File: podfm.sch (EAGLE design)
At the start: 30 parts, among them IC1 ATMEGA168-AU, IC2 FT232RL, X1 MINI-USB-32005-301, X2 R141426

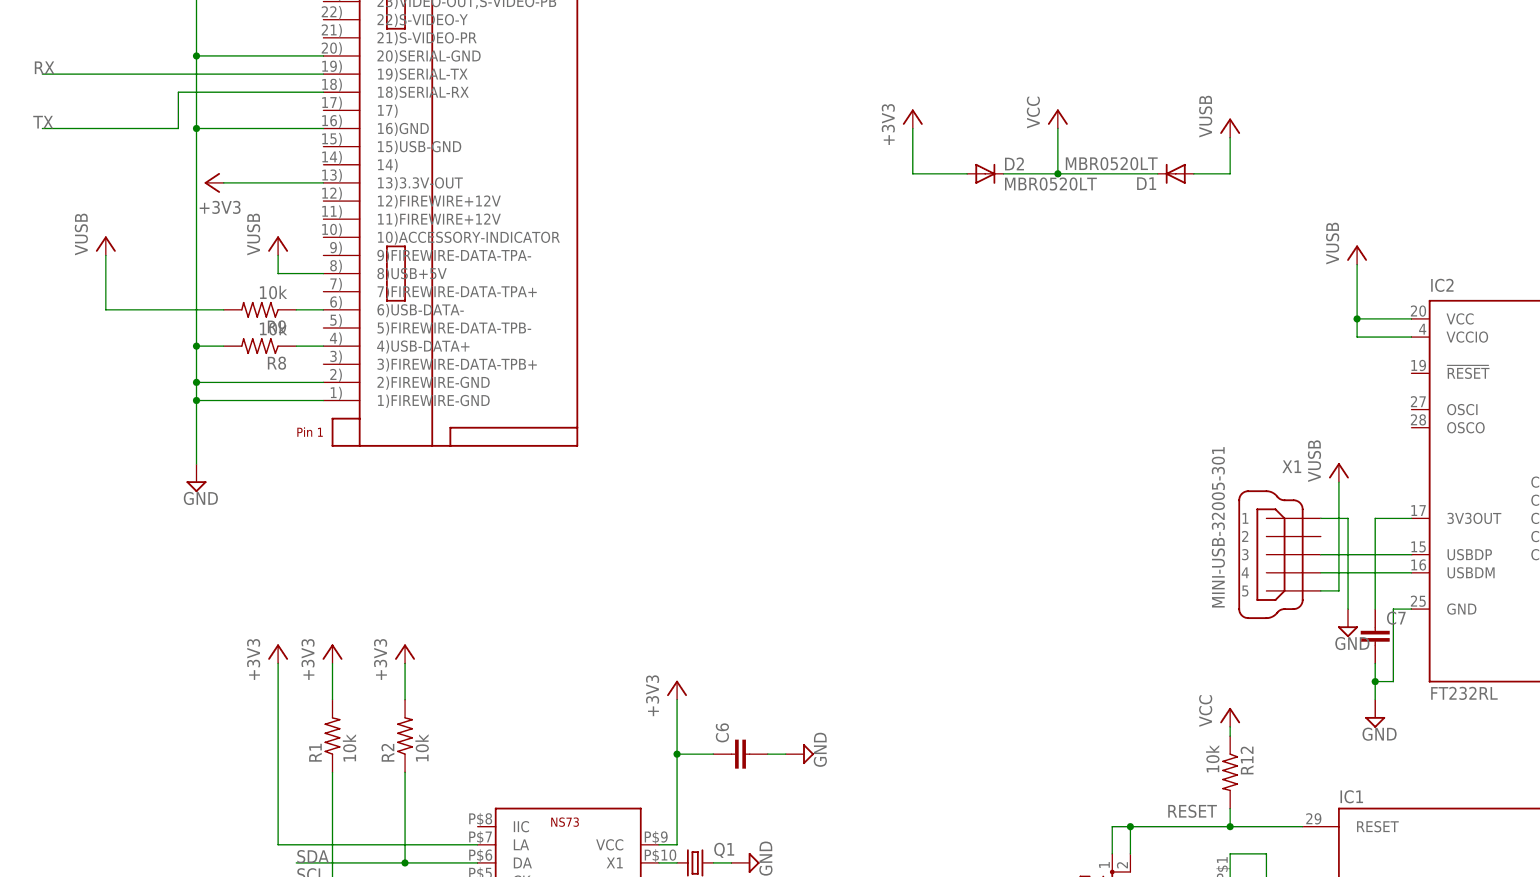
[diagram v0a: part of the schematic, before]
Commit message: 9/22/2013 fixed usb connection 1-VCC 2-data- 3-data+ 5-GND added resistor network for ipod iphone charging Signed-off-by: goose1987 <phamh1987@gmail.com>
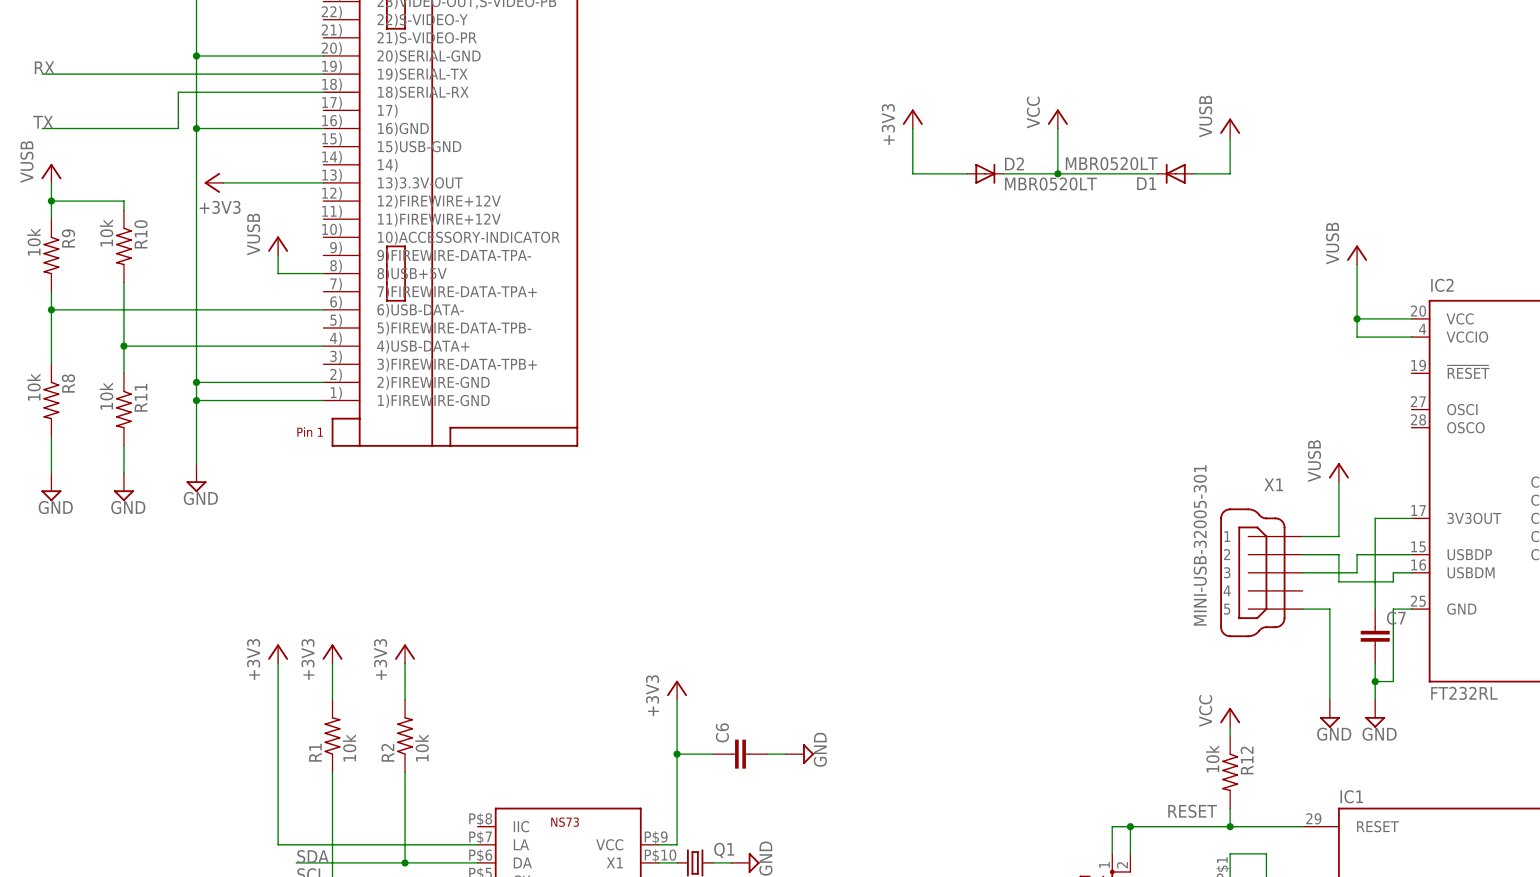
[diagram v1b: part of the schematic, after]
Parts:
- added R10, R11: 10k, rcl:R-US_R1206
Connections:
- net GND: now also R11.2, X1.5; no longer X1.1
- net N$3: now also X1.2; no longer X1.4
- net N$7: now also R10.2, R11.1; no longer R8.1
- net N$8: now also R8.1, R9.2; no longer R9.1
- net VUSB: now also R10.1, R9.1, X1.1; no longer R9.2, X1.5
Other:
- moved on the sheet: R8, R9, X1
